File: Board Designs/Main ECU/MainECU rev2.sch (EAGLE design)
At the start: 148 parts, among them X1 CONNECTOR-37, X2 CONNECTOR-4AUTOSPORT, X3 CONNECTOR-4NANO-FIT-VERTICAL-4, X4 CONNECTOR-4NANO-FIT-VERTICAL-4

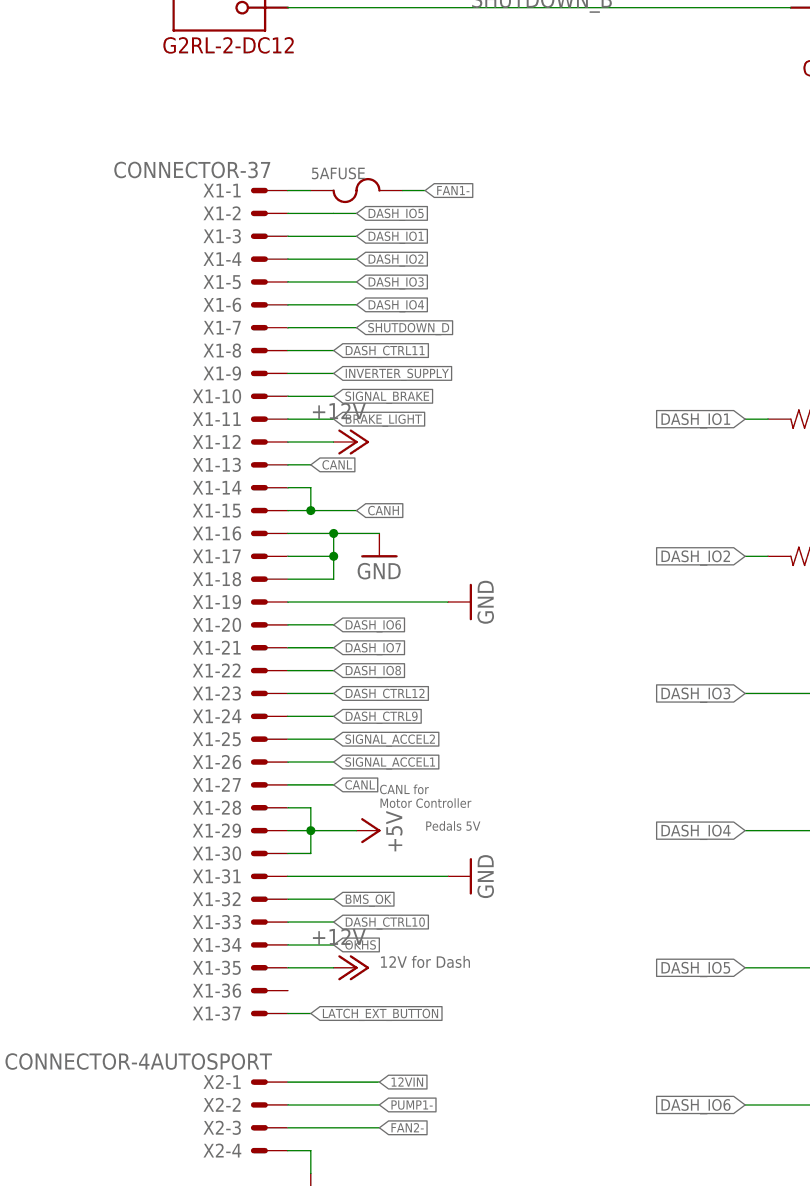
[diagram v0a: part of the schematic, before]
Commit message: Fixed Autosport Pinout on Main ECU
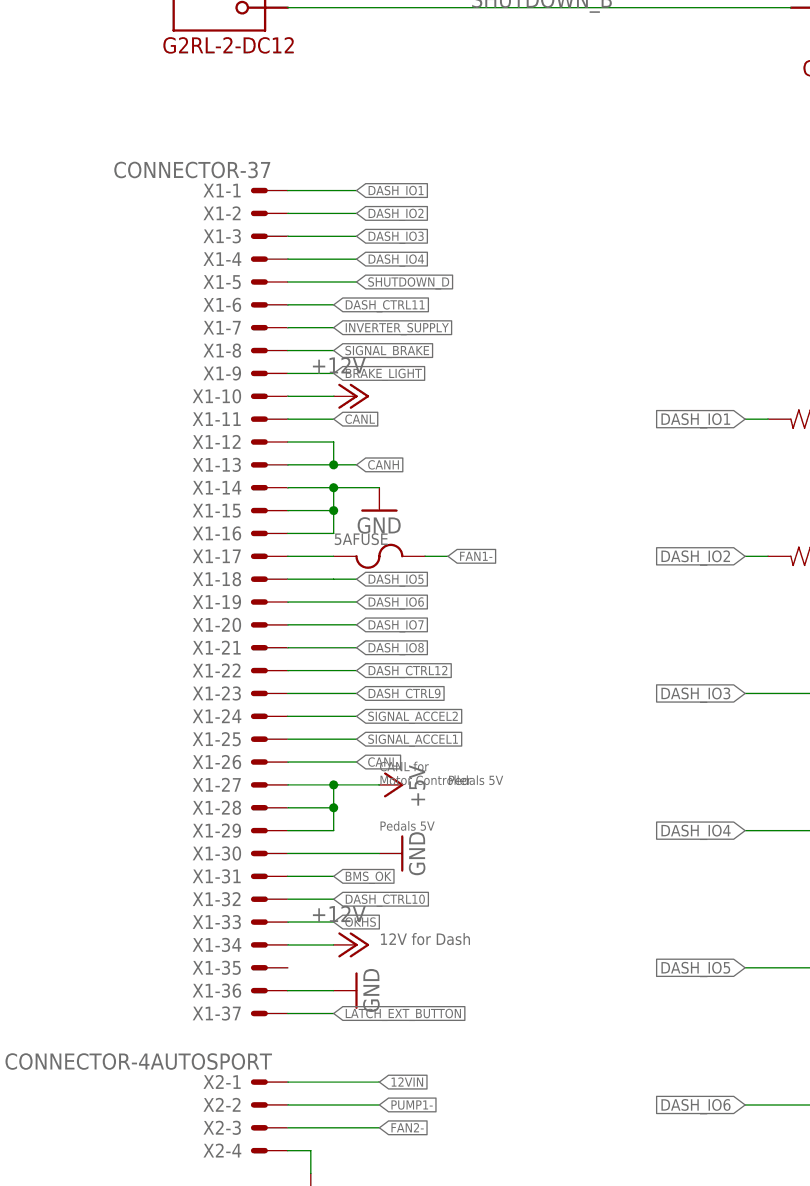
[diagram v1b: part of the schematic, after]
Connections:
- net +12V: now also X1-10.S, X1-34.S; no longer X1-12.S, X1-35.S
- net +5V: now also X1-27.S; no longer X1-30.S
- net BMS_OK: now also X1-31.S; no longer X1-32.S
- net BRAKE_LIGHT: now also X1-9.S; no longer X1-11.S
- net CANH: now also X1-12.S, X1-13.S; no longer X1-14.S, X1-15.S
- net CANL: now also X1-11.S, X1-26.S; no longer X1-13.S, X1-27.S
- net DASH_CTRL10: now also X1-32.S; no longer X1-33.S
- net DASH_CTRL11: now also X1-6.S; no longer X1-8.S
- net DASH_CTRL12: now also X1-22.S; no longer X1-23.S
- net DASH_CTRL9: now also X1-23.S; no longer X1-24.S
- net DASH_IO1: now also X1-1.S; no longer X1-3.S
- net DASH_IO2: now also X1-2.S; no longer X1-4.S
- net DASH_IO3: now also X1-3.S; no longer X1-5.S
- net DASH_IO4: now also X1-4.S; no longer X1-6.S
- net DASH_IO5: now also X1-18.S; no longer X1-2.S
- net DASH_IO6: now also X1-19.S; no longer X1-20.S
- net DASH_IO7: now also X1-20.S; no longer X1-21.S
- net DASH_IO8: now also X1-21.S; no longer X1-22.S
- net GND: now also X1-14.S, X1-15.S, X1-30.S, X1-36.S; no longer X1-17.S, X1-18.S, X1-19.S, X1-31.S
- net INVERTER_SUPPLY: now also X1-7.S; no longer X1-9.S
- net N$1: now also X1-17.S; no longer X1-1.S
- net OKHS: now also X1-33.S; no longer X1-34.S
- net SHUTDOWN_D: now also X1-5.S; no longer X1-7.S
- net SIGNAL_ACCEL1: now also X1-25.S; no longer X1-26.S
- net SIGNAL_ACCEL2: now also X1-24.S; no longer X1-25.S
- net SIGNAL_BRAKE: now also X1-8.S; no longer X1-10.S
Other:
- moved on the sheet: 5AFUSE

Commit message: Updated Rev 2 Schematic/Rev 1 Layout
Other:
- moved on the sheet: ACC1_PD, ACC1_PU, ACC2_PD, ACC2_PU, BOARD_TEMP, C11, C12, C14, C15, C16, C17, C18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

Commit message: Add transistor P/Ns to main ECU rev2 schematic
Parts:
- Q1, Q2, Q3, Q4, Q5, Q6, Q7, Q8: value (none) -> MMBT3904LT3G
- U$4, U$6, U$7: value N-CHANNEL_MOSFET_HOR_HOLE -> N-CHANNEL_MOSFET_FQP30N06L
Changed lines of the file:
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@@
 <part name="GND65" library="HyTechSymbols" deviceset="GND" device=""/>
 <part name="GND66" library="HyTechSymbols" deviceset="GND" device=""/>
-<part name="U$4" library="HyTechDevices" deviceset="N-CHANNEL_MOSFET" device="_HOR_HOLE"/>
-<part name="U$7" library="HyTechDevices" deviceset="N-CHANNEL_MOSFET" device="_HOR_HOLE"/>
-<part name="U$6" library="HyTechDevices" deviceset="N-CHANNEL_MOSFET" device="_HOR_HOLE"/>
+<part name="U$4" library="HyTechDevices" deviceset="N-CHANNEL_MOSFET" device="_HOR_HOLE" value="N-CHANNEL_MOSFET_FQP30N06L"/>
+<part name="U$7" library="HyTechDevices" deviceset="N-CHANNEL_MOSFET" device="_HOR_HOLE" value="N-CHANNEL_MOSFET_FQP30N06L"/>
+<part name="U$6" library="HyTechDevices" deviceset="N-CHANNEL_MOSFET" device="_HOR_HOLE" value="N-CHANNEL_MOSFET_FQP30N06L"/>
 <part name="R24" library="HyTechDevices" deviceset="RESISTOR" device="0805-RES" value="10k"/>
 <part name="R27" library="HyTechDevices" deviceset="RESISTOR" device="0805-RES" value="10k"/>
@@
 <part name="R39" library="HyTechDevices" deviceset="RESISTOR" device="0805-RES" value="2.2k"/>
 <part name="R40" library="HyTechDevices" deviceset="RESISTOR" device="0805-RES" value="2.2k"/>
-<part name="Q1" library="HyTechDevices" deviceset="BJT_NPN" device="SOT"/>
-<part name="Q2" library="HyTechDevices" deviceset="BJT_NPN" device="SOT"/>
-<part name="Q3" library="HyTechDevices" deviceset="BJT_NPN" device="SOT"/>
-<part name="Q4" library="HyTechDevices" deviceset="BJT_NPN" device="SOT"/>
-<part name="Q5" library="HyTechDevices" deviceset="BJT_NPN" device="SOT"/>
+<part name="Q1" library="HyTechDevices" deviceset="BJT_NPN" device="SOT" value="MMBT3904LT3G"/>
+<part name="Q2" library="HyTechDevices" deviceset="BJT_NPN" device="SOT" value="MMBT3904LT3G"/>
+<part name="Q3" library="HyTechDevices" deviceset="BJT_NPN" device="SOT" value="MMBT3904LT3G"/>
+<part name="Q4" library="HyTechDevices" deviceset="BJT_NPN" device="SOT" value="MMBT3904LT3G"/>
+<part name="Q5" library="HyTechDevices" deviceset="BJT_NPN" device="SOT" value="MMBT3904LT3G"/>
 <part name="GND37" library="HyTechSymbols" deviceset="GND" device=""/>
 <part name="P+30" library="supply1" deviceset="+12V" device=""/>
 <part name="R41" library="HyTechDevices" deviceset="RESISTOR" device="0805-RES" value="2.2k"/>
-<part name="Q6" library="HyTechDevices" deviceset="BJT_NPN" device="SOT"/>
+<part name="Q6" library="HyTechDevices" deviceset="BJT_NPN" device="SOT" value="MMBT3904LT3G"/>
 <part name="R42" library="HyTechDevices" deviceset="RESISTOR" device="0805-RES" value="2.2k"/>
-<part name="Q7" library="HyTechDevices" deviceset="BJT_NPN" device="SOT"/>
+<part name="Q7" library="HyTechDevices" deviceset="BJT_NPN" device="SOT" value="MMBT3904LT3G"/>
 <part name="R44" library="HyTechDevices" deviceset="RESISTOR" device="0805-RES" value="2.2k"/>
-<part name="Q8" library="HyTechDevices" deviceset="BJT_NPN" device="SOT"/>
+<part name="Q8" library="HyTechDevices" deviceset="BJT_NPN" device="SOT" value="MMBT3904LT3G"/>
 <part name="U$11" library="HyTechDevices" deviceset="JUMPER" device=""/>
 <part name="U$12" library="HyTechDevices" deviceset="JUMPER" device=""/>

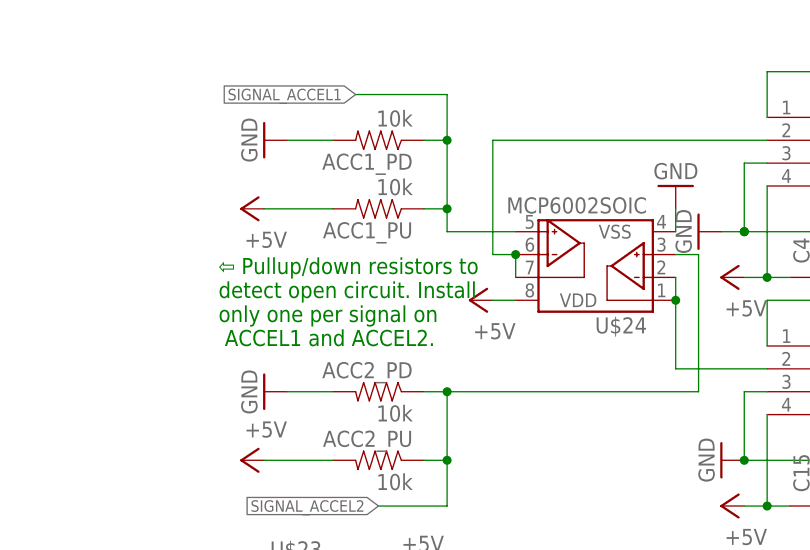
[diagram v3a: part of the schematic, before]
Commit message: Main ECU rev{1,2}: Update pullup/down resistor informational text, Main ECU rev1b: Update pinout to match Main ECU rev2
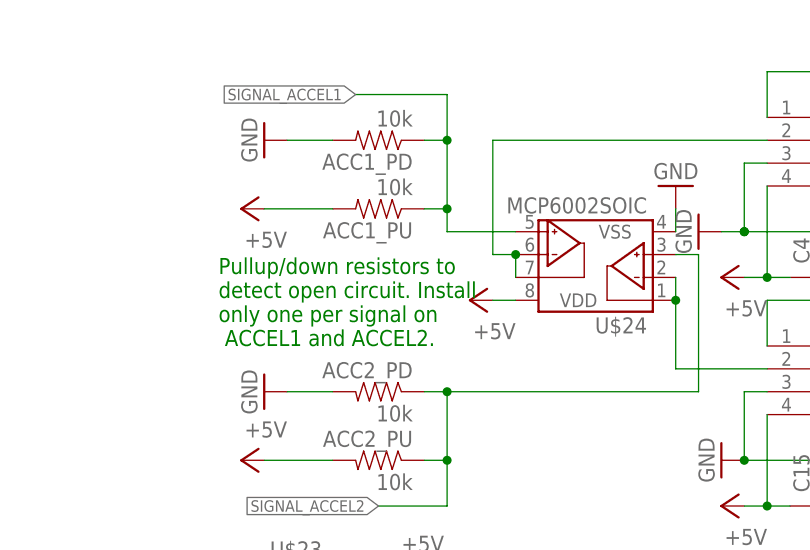
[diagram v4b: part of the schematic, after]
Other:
- note added: "Pullup/down resistors to detect open circuit. Install only one per signal on ACCEL1 and ACCEL2."
- note removed: "⇦ Pullup/down resistors to detect open circuit. Install only one per signal on ACCEL1 and ACCEL2."
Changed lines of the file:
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@@
 <text x="434.34" y="248.92" size="1.778" layer="97">ECU Current Sensor</text>
 <text x="426.72" y="200.66" size="1.778" layer="97">Cooling Current Sensor</text>
-<text x="266.7" y="233.68" size="1.778" layer="91">⇦ Pullup/down resistors to
+<text x="266.7" y="233.68" size="1.778" layer="91">Pullup/down resistors to
 detect open circuit. Install
 only one per signal on

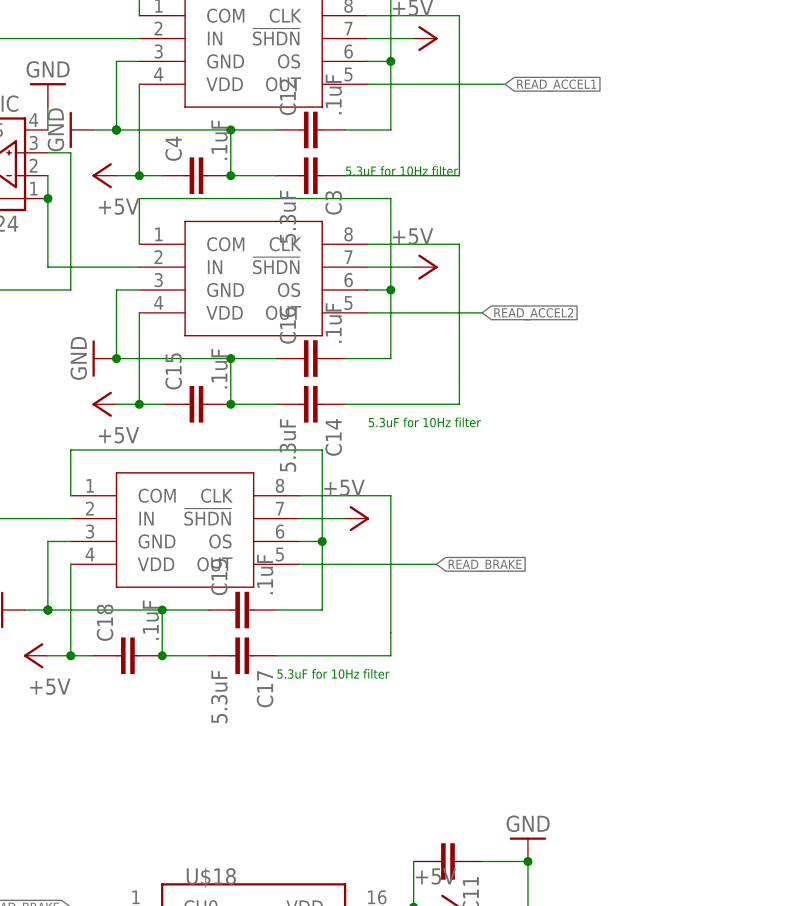
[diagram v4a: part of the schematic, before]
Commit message: Main ECU: [rev2, rev3] Fix filter frequency capacitor values, [rev1b, rev3] shorten a few traces
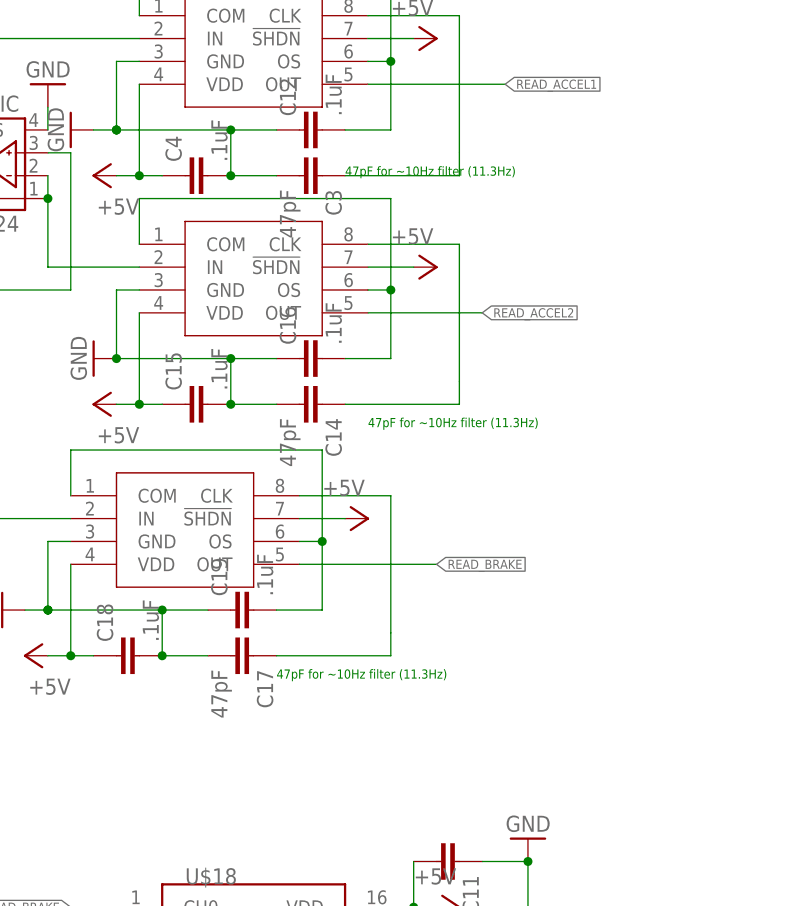
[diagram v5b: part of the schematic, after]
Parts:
- C14, C17, C3: value 5.3uF -> 47pF
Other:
- note added: "47pF for ~10Hz filter (11.3Hz)"
- note removed: "5.3uF for 10Hz filter"
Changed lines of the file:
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@@
 <part name="GND34" library="HyTechSymbols" deviceset="GND" device=""/>
 <part name="U$27" library="HyTechDevices" deviceset="MAX7480" device=""/>
-<part name="C3" library="HyTechDevices" deviceset="CAP" device="0805" value="5.3uF"/>
+<part name="C3" library="HyTechDevices" deviceset="CAP" device="0805" value="47pF"/>
 <part name="C4" library="HyTechDevices" deviceset="CAP" device="0805" value=".1uF"/>
 <part name="C12" library="HyTechDevices" deviceset="CAP" device="0805" value=".1uF"/>
@@
 <part name="P+15" library="supply1" library_urn="urn:adsk.eagle:library:371" deviceset="+5V" device=""/>
 <part name="U$28" library="HyTechDevices" deviceset="MAX7480" device=""/>
-<part name="C14" library="HyTechDevices" deviceset="CAP" device="0805" value="5.3uF"/>
+<part name="C14" library="HyTechDevices" deviceset="CAP" device="0805" value="47pF"/>
 <part name="C15" library="HyTechDevices" deviceset="CAP" device="0805" value=".1uF"/>
 <part name="C16" library="HyTechDevices" deviceset="CAP" device="0805" value=".1uF"/>
@@
 <part name="P+17" library="supply1" library_urn="urn:adsk.eagle:library:371" deviceset="+5V" device=""/>
 <part name="U$26" library="HyTechDevices" deviceset="MAX7480" device=""/>
-<part name="C17" library="HyTechDevices" deviceset="CAP" device="0805" value="5.3uF"/>
+<part name="C17" library="HyTechDevices" deviceset="CAP" device="0805" value="47pF"/>
 <part name="C18" library="HyTechDevices" deviceset="CAP" device="0805" value=".1uF"/>
 <part name="C19" library="HyTechDevices" deviceset="CAP" device="0805" value=".1uF"/>
@@
 <text x="58.42" y="93.98" size="1.016" layer="95">CANL for
 Motor Controller</text>
-<text x="350.52" y="241.3" size="1.016" layer="91">5.3uF for 10Hz filter</text>
-<text x="353.06" y="213.36" size="1.016" layer="91">5.3uF for 10Hz filter</text>
-<text x="342.9" y="185.42" size="1.016" layer="91">5.3uF for 10Hz filter</text>
+<text x="350.52" y="241.3" size="1.016" layer="91">47pF for ~10Hz filter (11.3Hz)</text>
+<text x="353.06" y="213.36" size="1.016" layer="91">47pF for ~10Hz filter (11.3Hz)</text>
+<text x="342.9" y="185.42" size="1.016" layer="91">47pF for ~10Hz filter (11.3Hz)</text>
 <text x="58.42" y="76.2" size="1.27" layer="96">12V for Dash</text>
 <text x="127" y="149.86" size="1.27" layer="96">Check Values, Switching V is 5V</text>

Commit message: Main ECU rev2: Fixed capacitor values *again* (I can't math)
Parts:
- C14, C17, C3: value 47pF -> 47nF
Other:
- note added: "47nF for ~10Hz filter (11.3Hz)"
- note removed: "47pF for ~10Hz filter (11.3Hz)"

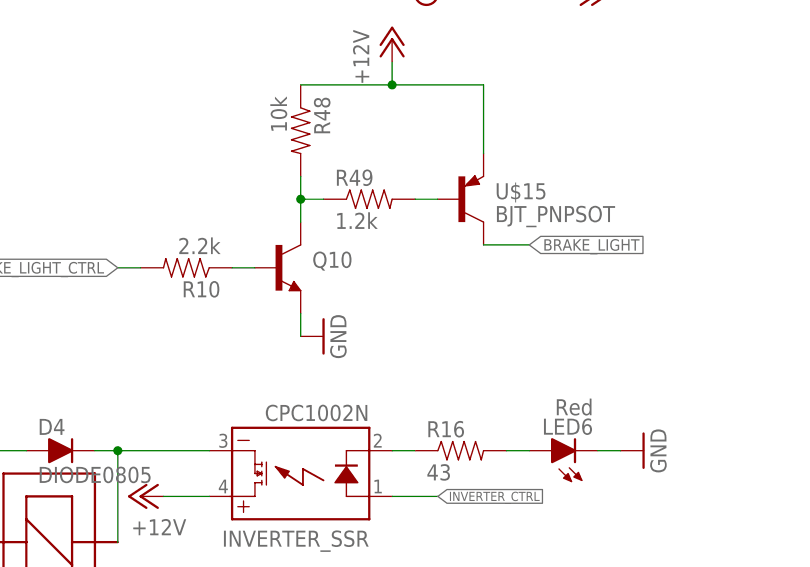
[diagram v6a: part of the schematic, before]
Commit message: Main ECU rev2/4: Add brake light NPN p/n
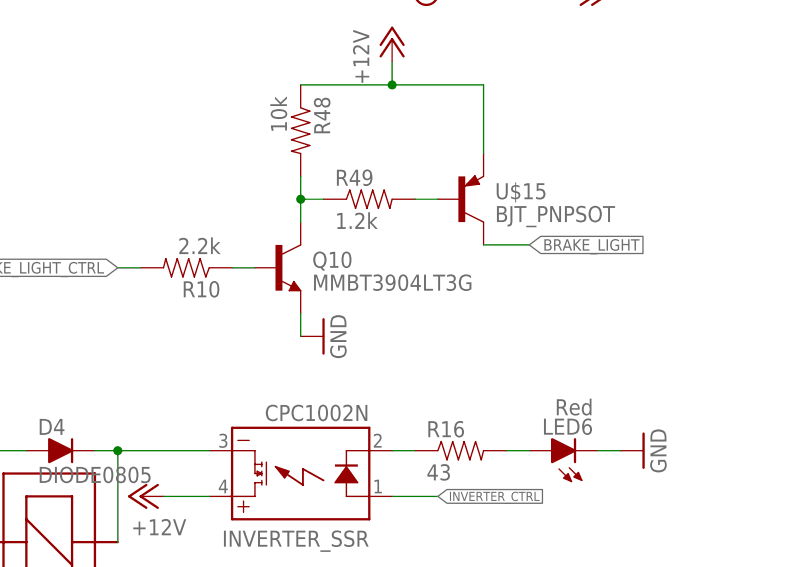
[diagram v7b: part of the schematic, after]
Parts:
- Q10: value (none) -> MMBT3904LT3G
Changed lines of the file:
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@@
 <part name="U$14" library="HyTechDevices" deviceset="JUMPER" device=""/>
 <part name="P+9" library="supply1" deviceset="+12V" device=""/>
-<part name="Q10" library="HyTechDevices" deviceset="BJT_NPN" device="SOT"/>
+<part name="Q10" library="HyTechDevices" deviceset="BJT_NPN" device="SOT" value="MMBT3904LT3G"/>
 <part name="U$15" library="HyTechDevices" deviceset="BJT_PNP" device="SOT"/>
 <part name="R10" library="HyTechDevices" deviceset="RESISTOR" device="0805-RES" value="2.2k"/>

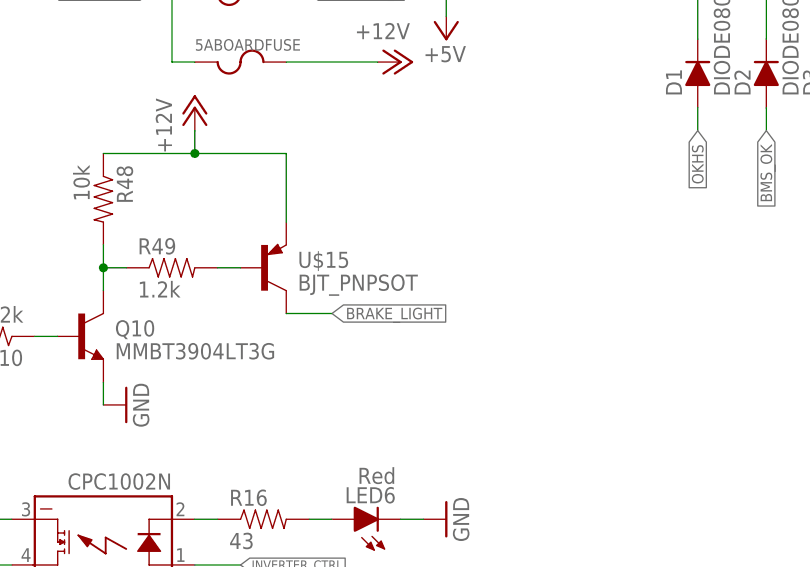
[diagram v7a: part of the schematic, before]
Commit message: Main ECU rev{2,4}: Specify PNP transistor P/Ns
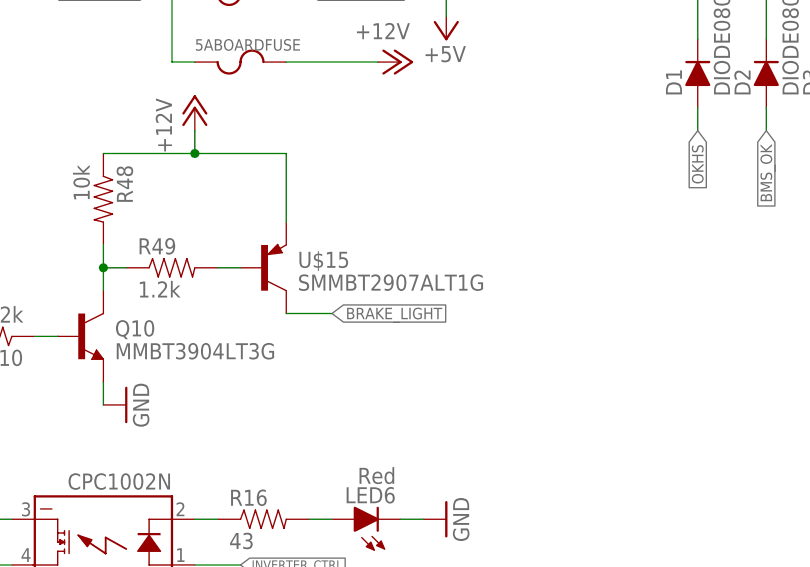
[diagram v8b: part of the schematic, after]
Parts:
- U$15: value BJT_PNPSOT -> SMMBT2907ALT1G
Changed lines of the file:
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@@
 <part name="P+9" library="supply1" deviceset="+12V" device=""/>
 <part name="Q10" library="HyTechDevices" deviceset="BJT_NPN" device="SOT" value="MMBT3904LT3G"/>
-<part name="U$15" library="HyTechDevices" deviceset="BJT_PNP" device="SOT"/>
+<part name="U$15" library="HyTechDevices" deviceset="BJT_PNP" device="SOT" value="SMMBT2907ALT1G"/>
 <part name="R10" library="HyTechDevices" deviceset="RESISTOR" device="0805-RES" value="2.2k"/>
 <part name="R48" library="HyTechDevices" deviceset="RESISTOR" device="0805-RES" value="10k"/>
